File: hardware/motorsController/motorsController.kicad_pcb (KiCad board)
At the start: 2 copper layers, 166.1 x 53.6 mm, 72 parts, among them J1 batery_connector, J10 batery_connector, J11 Conn_01x04, J2 Screw_Terminal_01x01, J3 Screw_Terminal_01x01, J4 Screw_Terminal_01x01, J5 Screw_Terminal_01x01, J6 Screw_Terminal_01x01, J7 Screw_Terminal_01x01, J8 Screw_Terminal_01x01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

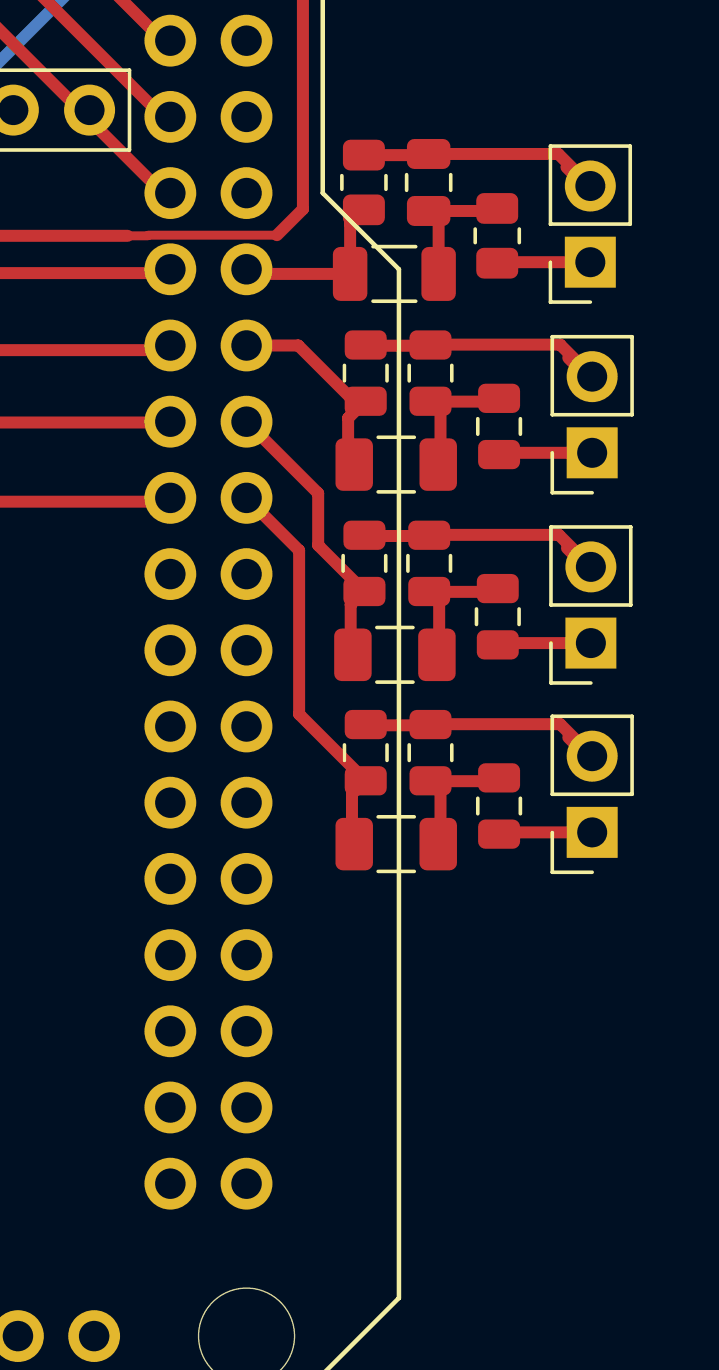
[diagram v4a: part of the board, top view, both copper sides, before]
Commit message: connect GNDs of encoders' filters to arduino's
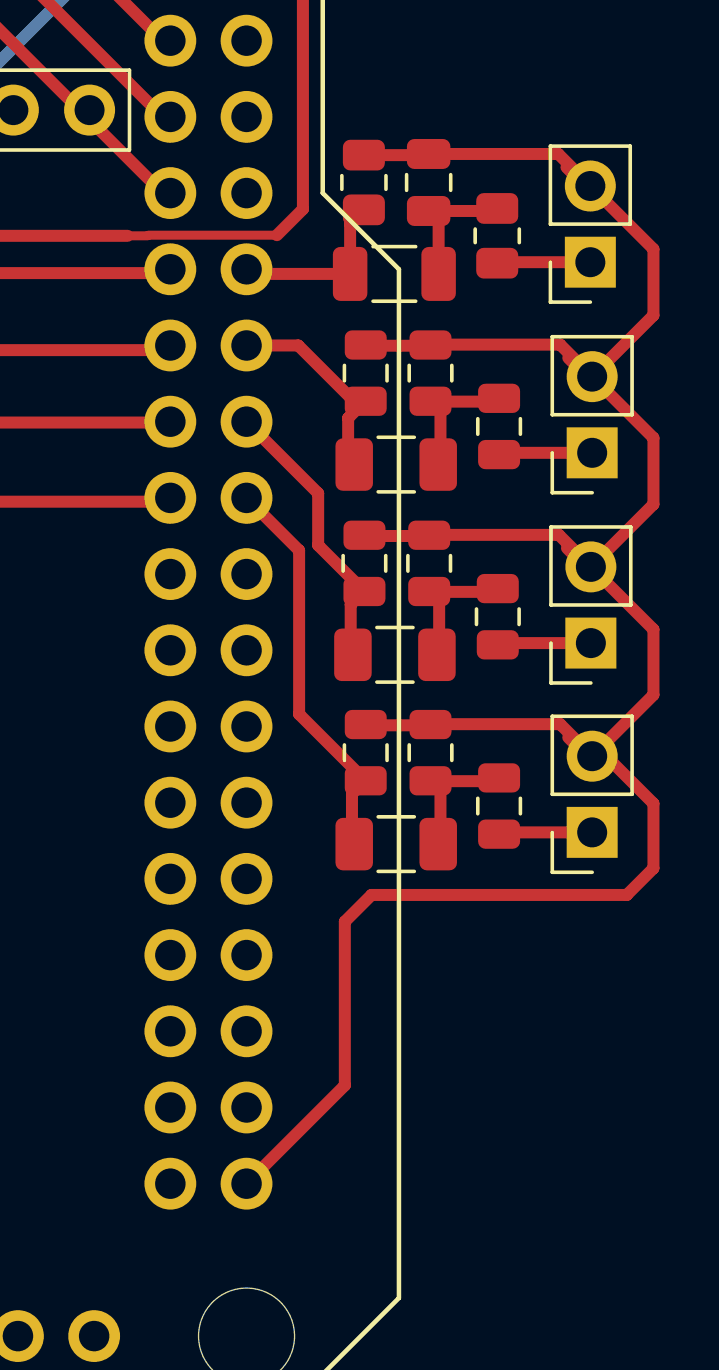
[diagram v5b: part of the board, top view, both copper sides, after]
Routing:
- net GND: track 680.8 -> 730.9 mm
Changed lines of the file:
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@@
     (thickness 1.6)
     (drawings 2)
-    (tracks 642)
+    (tracks 659)
     (zones 0)
     (modules 72)
@@
   (segment (start 205.1331 49.5161) (end 204.5081 48.8911) (width 0.4) (layer F.Cu) (net 1))
   (segment (start 205.3051 49.5161) (end 205.1331 49.5161) (width 0.4) (layer F.Cu) (net 1))
+  (segment (start 207.391 41.13168) (end 205.34834 43.17434) (width 0.4) (layer F.Cu) (net 1))
+  (segment (start 207.391 38.924) (end 207.391 41.13168) (width 0.4) (layer F.Cu) (net 1))
+  (segment (start 205.287 36.82) (end 207.391 38.924) (width 0.4) (layer F.Cu) (net 1))
+  (segment (start 207.391 47.4302) (end 205.3051 49.5161) (width 0.4) (layer F.Cu) (net 1))
+  (segment (start 207.391 45.217) (end 207.391 47.4302) (width 0.4) (layer F.Cu) (net 1))
+  (segment (start 205.34834 43.17434) (end 207.391 45.217) (width 0.4) (layer F.Cu) (net 1))
+  (segment (start 207.391 53.78366) (end 205.34858 55.82608) (width 0.4) (layer F.Cu) (net 1))
+  (segment (start 207.391 51.602) (end 207.391 53.78366) (width 0.4) (layer F.Cu) (net 1))
+  (segment (start 205.3051 49.5161) (end 207.391 51.602) (width 0.4) (layer F.Cu) (net 1))
+  (segment (start 197.104 66.79946) (end 193.8274 70.07606) (width 0.4) (layer F.Cu) (net 1))
+  (segment (start 197.993 60.452) (end 197.104 61.341) (width 0.4) (layer F.Cu) (net 1))
+  (segment (start 206.502 60.452) (end 197.993 60.452) (width 0.4) (layer F.Cu) (net 1))
+  (segment (start 207.391 59.563) (end 206.502 60.452) (width 0.4) (layer F.Cu) (net 1))
+  (segment (start 197.104 61.341) (end 197.104 66.79946) (width 0.4) (layer F.Cu) (net 1))
+  (segment (start 207.391 57.404) (end 207.391 59.563) (width 0.4) (layer F.Cu) (net 1))
+  (segment (start 205.81308 55.82608) (end 207.391 57.404) (width 0.4) (layer F.Cu) (net 1))
+  (segment (start 205.34858 55.82608) (end 205.81308 55.82608) (width 0.4) (layer F.Cu) (net 1))
   (segment (start 49.345001 42.499999) (end 58.655 42.499999) (width 1) (layer F.Cu) (net 2))
   (segment (start 46.48 45.365) (end 49.345001 42.499999) (width 1) (layer F.Cu) (net 2))

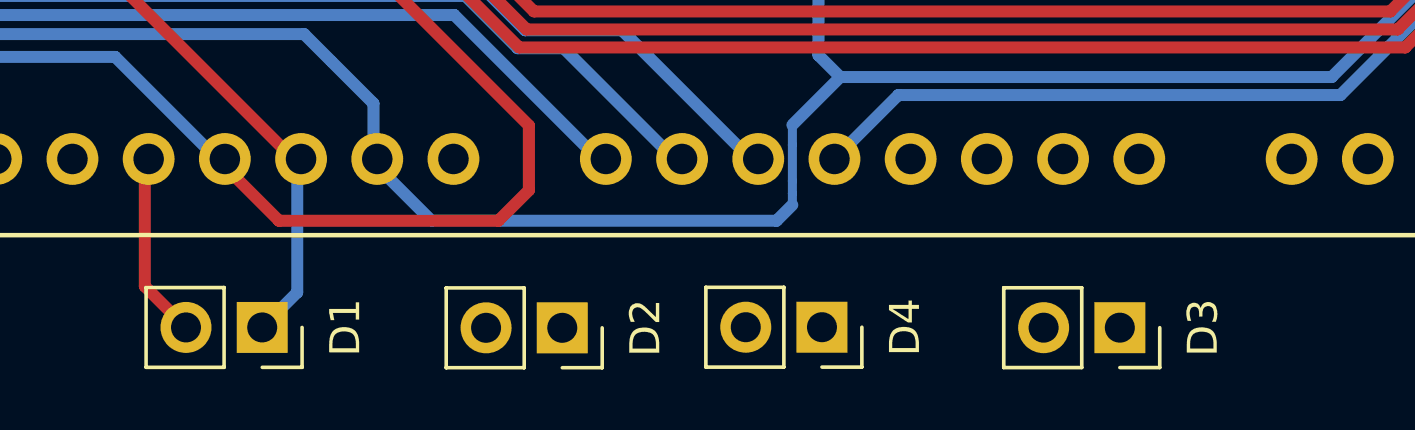
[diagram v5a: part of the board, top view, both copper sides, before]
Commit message: eonnect power for the rest of encoders' leds
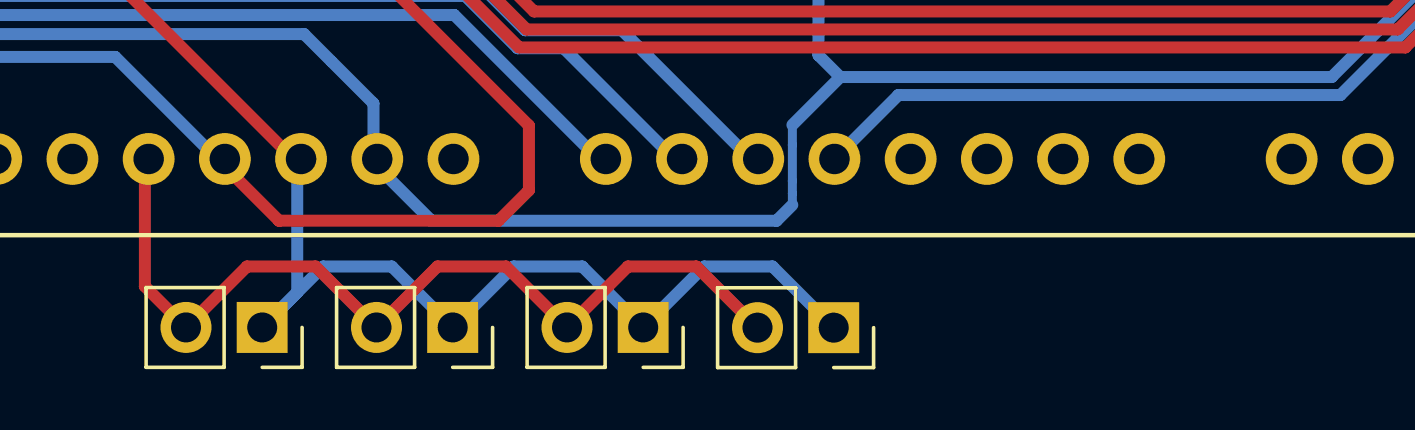
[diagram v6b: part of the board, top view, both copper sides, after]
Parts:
- moved D3 9.54 mm to (155.7, 80.8)
- moved D4 5.96 mm to (149.4, 80.8)
- moved D2 3.65 mm to (143.0, 80.8)
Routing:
- net GND: track 730.9 -> 755.0 mm
- net +3V3: track 6.06 -> 30.2 mm
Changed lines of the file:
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@@
     (thickness 1.6)
     (drawings 2)
-    (tracks 659)
+    (tracks 677)
     (zones 0)
     (modules 72)
@@
   )
   (module Connector_PinSocket_2.54mm:PinSocket_1x02_P2.54mm_Vertical (layer F.Cu)
-    (at 155.31084 80.76438 270)
+    (at 149.352 80.772 270)
     (descr "Through hole straight socket strip, 1x02, 2.54mm pitch, single row (from Kicad 4.0.7), script generated")
     (tags "Through hole socket strip THT 1x02 2.54mm single row")
-    (fp_text reference D4 (at 0 -2.77 270) (layer F.SilkS)
+    (fp_text reference D4 (at 0 -2.77 270) (layer F.SilkS) hide
       (effects (font (size 1 1) (thickness 0.15)))
     )
-    (fp_text value LED (at 0 5.31 270) (layer F.Fab)
+    (fp_text value LED (at 0 5.31 270) (layer F.Fab) hide
       (effects (font (size 1 1) (thickness 0.15)))
     )
@@
     (fp_line (start 0.635 -1.27) (end 1.27 -0.635) (layer F.Fab) (width 0.1))
     (fp_line (start -1.27 -1.27) (end 0.635 -1.27) (layer F.Fab) (width 0.1))
-    (fp_text user %R (at 0 1.27 180) (layer F.Fab)
+    (fp_text user %R (at 0 1.27 180) (layer F.Fab) hide
       (effects (font (size 1 1) (thickness 0.15)))
     )
@@
   )
   (module Connector_PinSocket_2.54mm:PinSocket_1x02_P2.54mm_Vertical (layer F.Cu)
-    (at 165.2397 80.77962 270)
+    (at 155.702 80.77962 270)
     (descr "Through hole straight socket strip, 1x02, 2.54mm pitch, single row (from Kicad 4.0.7), script generated")
     (tags "Through hole socket strip THT 1x02 2.54mm single row")
-    (fp_text reference D3 (at 0 -2.77 270) (layer F.SilkS)
+    (fp_text reference D3 (at 0 -2.77 270) (layer F.SilkS) hide
       (effects (font (size 1 1) (thickness 0.15)))
     )
-    (fp_text value LED (at 0 5.31 270) (layer F.Fab)
+    (fp_text value LED (at 0 5.31 270) (layer F.Fab) hide
       (effects (font (size 1 1) (thickness 0.15)))
     )
@@
     (fp_line (start 0.635 -1.27) (end 1.27 -0.635) (layer F.Fab) (width 0.1))
     (fp_line (start -1.27 -1.27) (end 0.635 -1.27) (layer F.Fab) (width 0.1))
-    (fp_text user %R (at 0 1.27 180) (layer F.Fab)
+    (fp_text user %R (at 0 1.27 180) (layer F.Fab) hide
       (effects (font (size 1 1) (thickness 0.15)))
     )
@@
   )
   (module Connector_PinSocket_2.54mm:PinSocket_1x02_P2.54mm_Vertical (layer F.Cu)
-    (at 146.65452 80.7847 270)
+    (at 143.002 80.772 270)
     (descr "Through hole straight socket strip, 1x02, 2.54mm pitch, single row (from Kicad 4.0.7), script generated")
     (tags "Through hole socket strip THT 1x02 2.54mm single row")
-    (fp_text reference D2 (at 0 -2.77 270) (layer F.SilkS)
+    (fp_text reference D2 (at 0 -2.77 270) (layer F.SilkS) hide
       (effects (font (size 1 1) (thickness 0.15)))
     )
-    (fp_text value LED (at 0 5.31 270) (layer F.Fab)
+    (fp_text value LED (at 0 5.31 270) (layer F.Fab) hide
       (effects (font (size 1 1) (thickness 0.15)))
     )
@@
     (fp_line (start 0.635 -1.27) (end 1.27 -0.635) (layer F.Fab) (width 0.1))
     (fp_line (start -1.27 -1.27) (end 0.635 -1.27) (layer F.Fab) (width 0.1))
-    (fp_text user %R (at 0 1.27 180) (layer F.Fab)
+    (fp_text user %R (at 0 1.27 180) (layer F.Fab) hide
       (effects (font (size 1 1) (thickness 0.15)))
     )
@@
     (descr "Through hole straight socket strip, 1x02, 2.54mm pitch, single row (from Kicad 4.0.7), script generated")
     (tags "Through hole socket strip THT 1x02 2.54mm single row")
-    (fp_text reference D1 (at 0 -2.77 90) (layer F.SilkS)
+    (fp_text reference D1 (at 0 -2.77 90) (layer F.SilkS) hide
       (effects (font (size 1 1) (thickness 0.15)))
     )
-    (fp_text value LED (at 0 5.31 90) (layer F.Fab)
+    (fp_text value LED (at 0 5.31 90) (layer F.Fab) hide
       (effects (font (size 1 1) (thickness 0.15)))
     )
@@
     (fp_line (start 0.635 -1.27) (end 1.27 -0.635) (layer F.Fab) (width 0.1))
     (fp_line (start -1.27 -1.27) (end 0.635 -1.27) (layer F.Fab) (width 0.1))
-    (fp_text user %R (at 0 1.27) (layer F.Fab)
+    (fp_text user %R (at 0 1.27) (layer F.Fab) hide
       (effects (font (size 1 1) (thickness 0.15)))
     )
@@
   (segment (start 205.81308 55.82608) (end 207.391 57.404) (width 0.4) (layer F.Cu) (net 1))
   (segment (start 205.34858 55.82608) (end 205.81308 55.82608) (width 0.4) (layer F.Cu) (net 1))
+  (segment (start 140.97 78.74) (end 143.002 80.772) (width 0.4) (layer B.Cu) (net 1))
+  (segment (start 138.684 78.74) (end 140.97 78.74) (width 0.4) (layer B.Cu) (net 1))
+  (segment (start 136.652 80.772) (end 138.684 78.74) (width 0.4) (layer B.Cu) (net 1))
+  (segment (start 147.32 78.74) (end 149.352 80.772) (width 0.4) (layer B.Cu) (net 1))
+  (segment (start 145.034 78.74) (end 147.32 78.74) (width 0.4) (layer B.Cu) (net 1))
+  (segment (start 143.002 80.772) (end 145.034 78.74) (width 0.4) (layer B.Cu) (net 1))
+  (segment (start 153.66238 78.74) (end 155.702 80.77962) (width 0.4) (layer B.Cu) (net 1))
+  (segment (start 151.384 78.74) (end 153.66238 78.74) (width 0.4) (layer B.Cu) (net 1))
+  (segment (start 149.352 80.772) (end 151.384 78.74) (width 0.4) (layer B.Cu) (net 1))
   (segment (start 49.345001 42.499999) (end 58.655 42.499999) (width 1) (layer F.Cu) (net 2))
   (segment (start 46.48 45.365) (end 49.345001 42.499999) (width 1) (layer F.Cu) (net 2))
@@
   (segment (start 132.7404 79.4004) (end 134.112 80.772) (width 0.4) (layer F.Cu) (net 138))
   (segment (start 132.7404 75.28306) (end 132.7404 79.4004) (width 0.4) (layer F.Cu) (net 138))
+  (segment (start 136.144 78.74) (end 138.43 78.74) (width 0.4) (layer F.Cu) (net 138))
+  (segment (start 138.43 78.74) (end 140.462 80.772) (width 0.4) (layer F.Cu) (net 138))
+  (segment (start 134.112 80.772) (end 136.144 78.74) (width 0.4) (layer F.Cu) (net 138))
+  (segment (start 144.78 78.74) (end 146.812 80.772) (width 0.4) (layer F.Cu) (net 138))
+  (segment (start 142.494 78.74) (end 144.78 78.74) (width 0.4) (layer F.Cu) (net 138))
+  (segment (start 140.462 80.772) (end 142.494 78.74) (width 0.4) (layer F.Cu) (net 138))
+  (segment (start 151.12238 78.74) (end 153.162 80.77962) (width 0.4) (layer F.Cu) (net 138))
+  (segment (start 148.844 78.74) (end 151.12238 78.74) (width 0.4) (layer F.Cu) (net 138))
+  (segment (start 146.812 80.772) (end 148.844 78.74) (width 0.4) (layer F.Cu) (net 138))
   (segment (start 202.194 39.36) (end 202.184 39.37) (width 0.25) (layer F.Cu) (net 139))
   (segment (start 202.2175 39.36) (end 202.184 39.3935) (width 0.4) (layer F.Cu) (net 139))
